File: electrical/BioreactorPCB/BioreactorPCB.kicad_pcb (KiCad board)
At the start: 2 copper layers, 81.5 x 56.5 mm, 68 parts, among them IC1 AL5809-20P1-7, IC2 VEML7700-TR, J1 61300311121, J10 USB_B, J11 Conn_01x06_Male, J12 Conn_02x03_Odd_Even, J13 PJ-202A, J14 Conn_01x05_Male, J2 61300311121, J3 Conn_01x05_Male, J4 Conn_01x06_Male, J5 OSTTC022162, J6 OSTTC022162, J7 OSTTC042162, J8 OSTTC042162, J9 OSTTC042162, Q1 2N3905, Q2 IRF540N, Q3 FQP47P06, Q4 TL2575HV-05IKV, U1 L293D, U2 FT232RL, U3 ATMEGA328P-AUR, U4 TCA39306DCUR, Y1 16 mHz

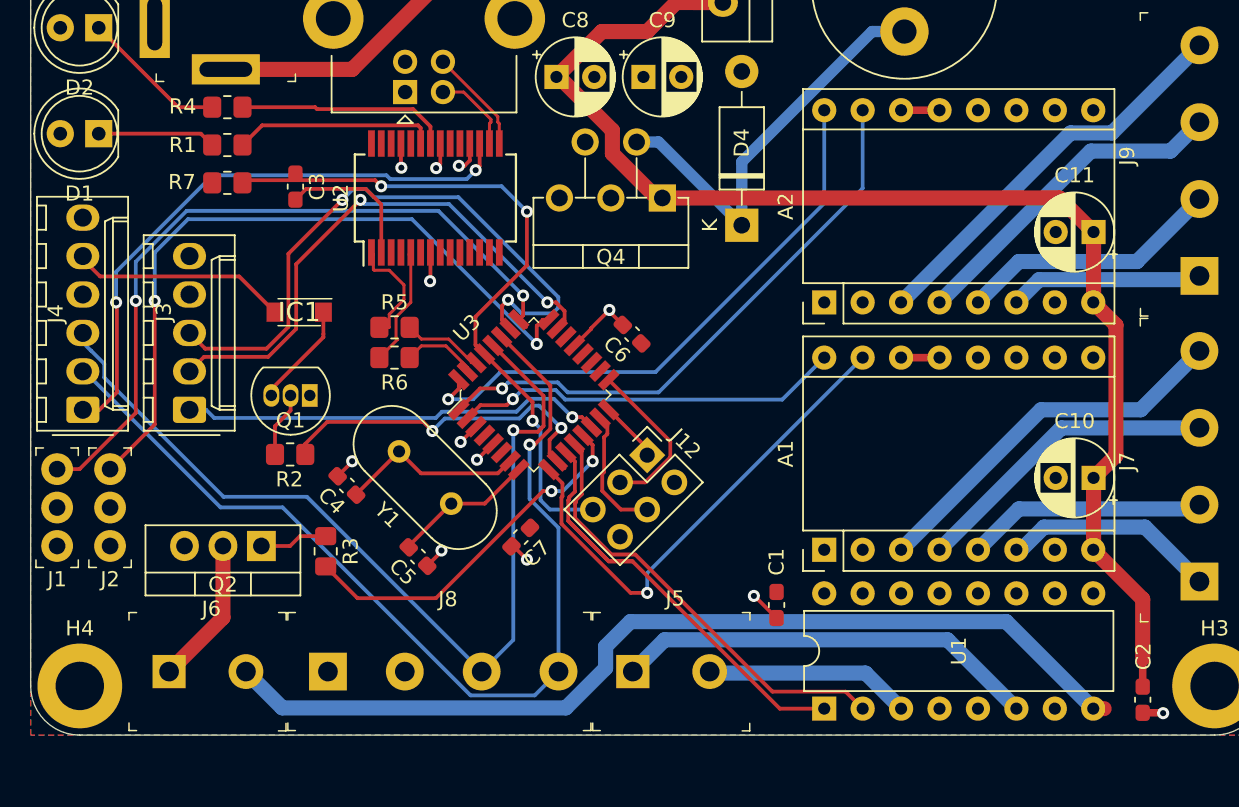
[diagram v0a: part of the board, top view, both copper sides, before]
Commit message: Moved around some traces for better planes
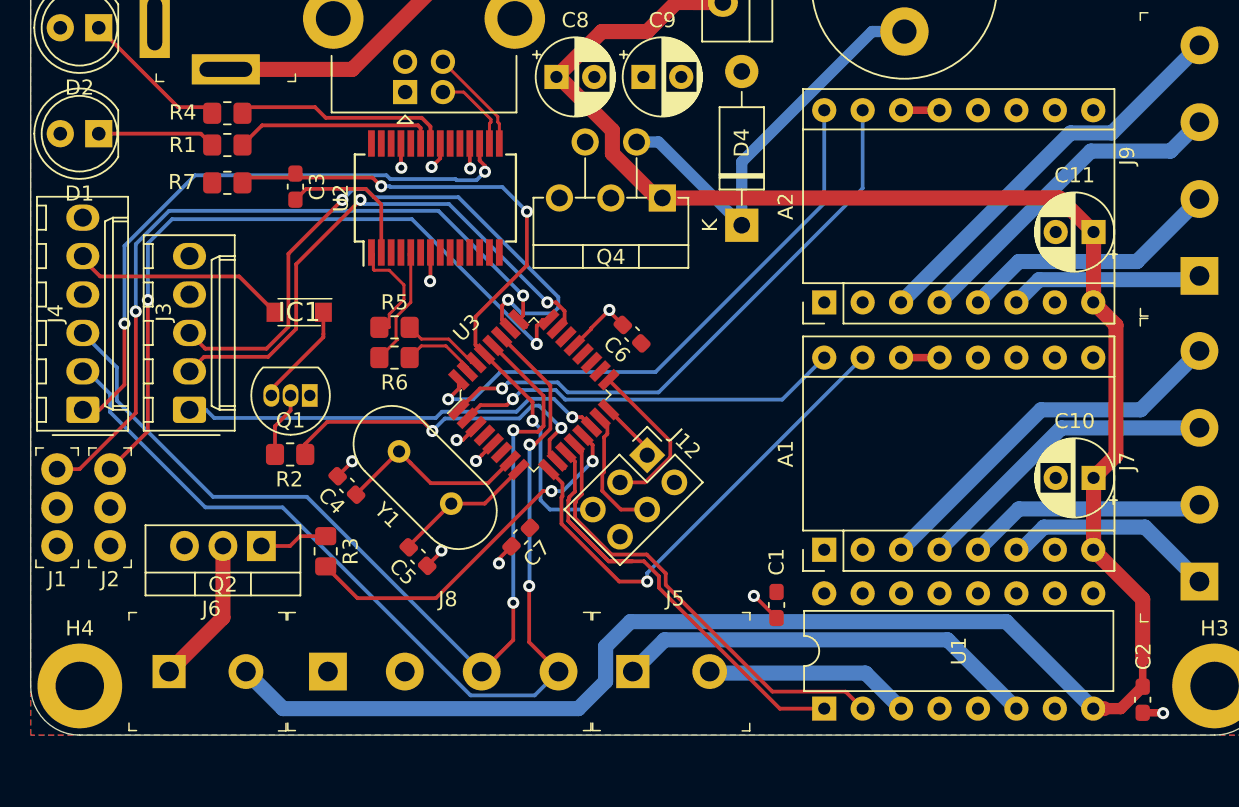
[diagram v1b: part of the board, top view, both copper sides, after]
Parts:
- moved R4 0.40 mm to (94.8, 52.9)
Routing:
- net +12V: track 151.6 -> 156.1 mm
- net +3V3: track 39.4 -> 40.8 mm
- net D5: track 33.0 -> 31.9 mm
- net SDA: track 66.8 -> 67.5 mm, vias 1 -> 2
- net TEMP_OUT: track 48.4 -> 49.1 mm
- net PH_OUT: track 47.3 -> 47.9 mm
- net XTAL+: track 12.3 -> 12.9 mm
- net SCL: track 62.2 -> 62.7 mm, vias 1 -> 2

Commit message: finished daughterboards
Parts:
- J11, J14, R8, U4: moved to B.Cu
- moved H6 118.4 mm to (114.2, 97.7), turned to 270 degrees
- moved H5 104.5 mm to (114.2, 117.7), turned to 270 degrees
- moved H10 98.9 mm to (85.0, 97.7), turned to 90 degrees
- moved R8 97.8 mm to (120.0, 102.5)
- moved U4 96.5 mm to (130.0, 102.3), turned to 180 degrees
- moved D3 87.2 mm to (114.2, 109.0), turned to 90 degrees
- moved H9 87.1 mm to (85.0, 117.7), turned to 90 degrees
- moved H12 84.4 mm to (107.5, 97.7), turned to 90 degrees
- moved J14 83.8 mm to (85.2, 112.8), turned to 90 degrees
- moved R10 81.7 mm to (90.5, 102.8), turned to 270 degrees
- moved R11 79.7 mm to (90.5, 112.7), turned to 90 degrees
- moved H11 77.1 mm to (107.5, 117.7), turned to 90 degrees
- moved H7 75.0 mm to (144.2, 97.7)
- moved R9 69.4 mm to (90.5, 107.7), turned to 90 degrees
- moved H8 66.2 mm to (144.2, 117.7)
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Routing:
- net Net-(J14-Pad3): track 0.00 -> 25.3 mm
- net Net-(J14-Pad2): track 0.00 -> 24.9 mm, vias 0 -> 1
- net 3V3_2: track 0.00 -> 21.7 mm
- net Net-(J14-Pad1): track 0.00 -> 18.3 mm
- net SCL1: track 0.00 -> 17.3 mm, vias 0 -> 1
- net Net-(D3-Pad2): track 0.00 -> 15.0 mm
- net SDA1: track 0.00 -> 12.9 mm, vias 0 -> 1
- net SDA2: track 0.00 -> 9.41 mm, vias 0 -> 1
- net Net-(R8-Pad2): track 0.00 -> 8.31 mm
- net 5V_3: track 0.00 -> 6.35 mm
- net SCL2: track 0.00 -> 6.09 mm
- net Net-(D4-Pad1): track 27.7 -> 28.3 mm
- net D2: track 37.9 -> 37.4 mm
- net GND2: vias 0 -> 1
- added copper zone on F.Cu, net 5V_2
- added copper zone on B.Cu, net GND2
- added copper zone on F.Cu, net GND2
- added copper zone on B.Cu, net GND3
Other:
- board size 81.5 x 56.5 mm -> 81.5 x 83.4 mm

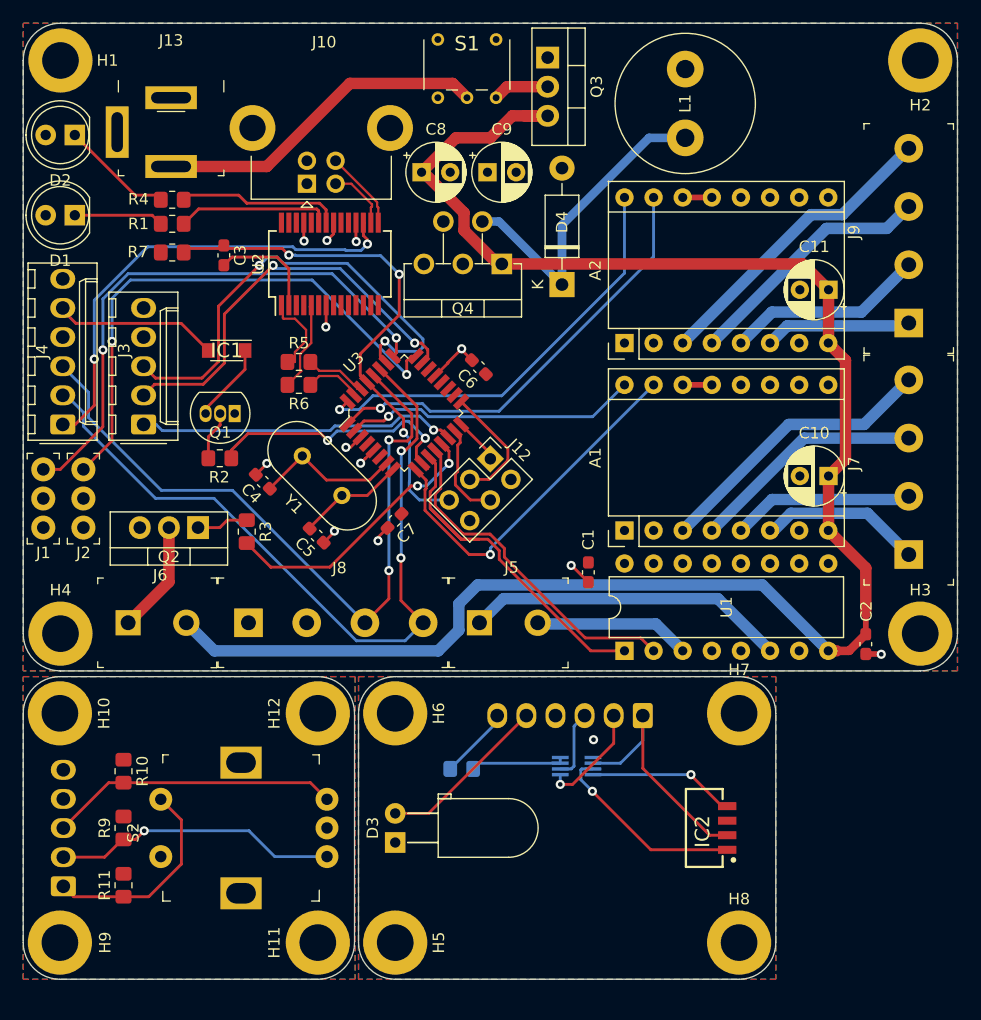
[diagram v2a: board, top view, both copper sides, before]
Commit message: panelized completed daughterboards and added clearance of planes to board edge
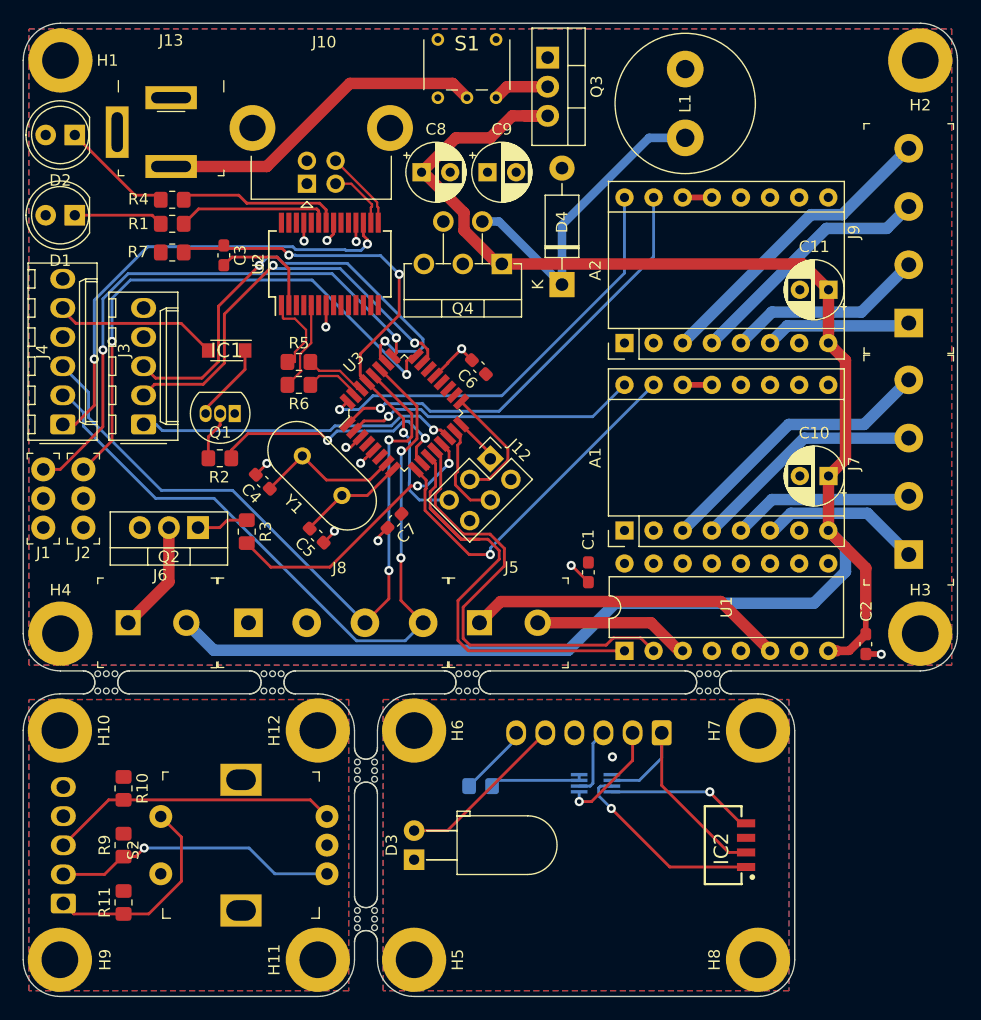
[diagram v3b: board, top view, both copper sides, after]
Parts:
- added mouse-bite-2mm-slot: VAL**, Panelization:mouse-bite-2mm-slot, F.Cu at (111.7, 115.7)
- added mouse-bite-2mm-slot: VAL**, Panelization:mouse-bite-2mm-slot, F.Cu at (111.7, 102.7)
- added mouse-bite-2mm-slot: VAL**, Panelization:mouse-bite-2mm-slot, F.Cu at (141.5, 95.0)
- added mouse-bite-2mm-slot: VAL**, Panelization:mouse-bite-2mm-slot, F.Cu at (120.5, 95.0)
- added mouse-bite-2mm-slot: VAL**, Panelization:mouse-bite-2mm-slot, F.Cu at (103.5, 95.0)
- added mouse-bite-2mm-slot: VAL**, Panelization:mouse-bite-2mm-slot, F.Cu at (89.0, 95.0)
- moved H7 2.23 mm to (145.8, 99.2), turned to 90 degrees
- moved H8 2.23 mm to (145.8, 119.2), turned to 90 degrees
- moved IC2 2.23 mm to (144.4, 112.6)
- moved R8 2.23 mm to (121.7, 104.0)
- moved U4 2.23 mm to (131.7, 103.8)
- moved D3 2.23 mm to (115.8, 110.5)
- moved H5 2.23 mm to (115.8, 119.2)
- moved H6 2.23 mm to (115.8, 99.2)
- moved J11 2.23 mm to (137.4, 99.4)
- moved H10 1.50 mm to (85.0, 99.2)
- moved H11 1.50 mm to (107.5, 119.2)
- moved H12 1.50 mm to (107.5, 99.2)
- moved H9 1.50 mm to (85.0, 119.2)
- moved J14 1.50 mm to (85.2, 114.3)
- moved R10 1.50 mm to (90.5, 104.2)
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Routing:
- net D8: track 30.0 -> 39.7 mm
- net D7: track 33.5 -> 42.8 mm
- net +12V: track 156.1 -> 158.5 mm
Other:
- board size 81.5 x 83.4 mm -> 81.5 x 84.9 mm

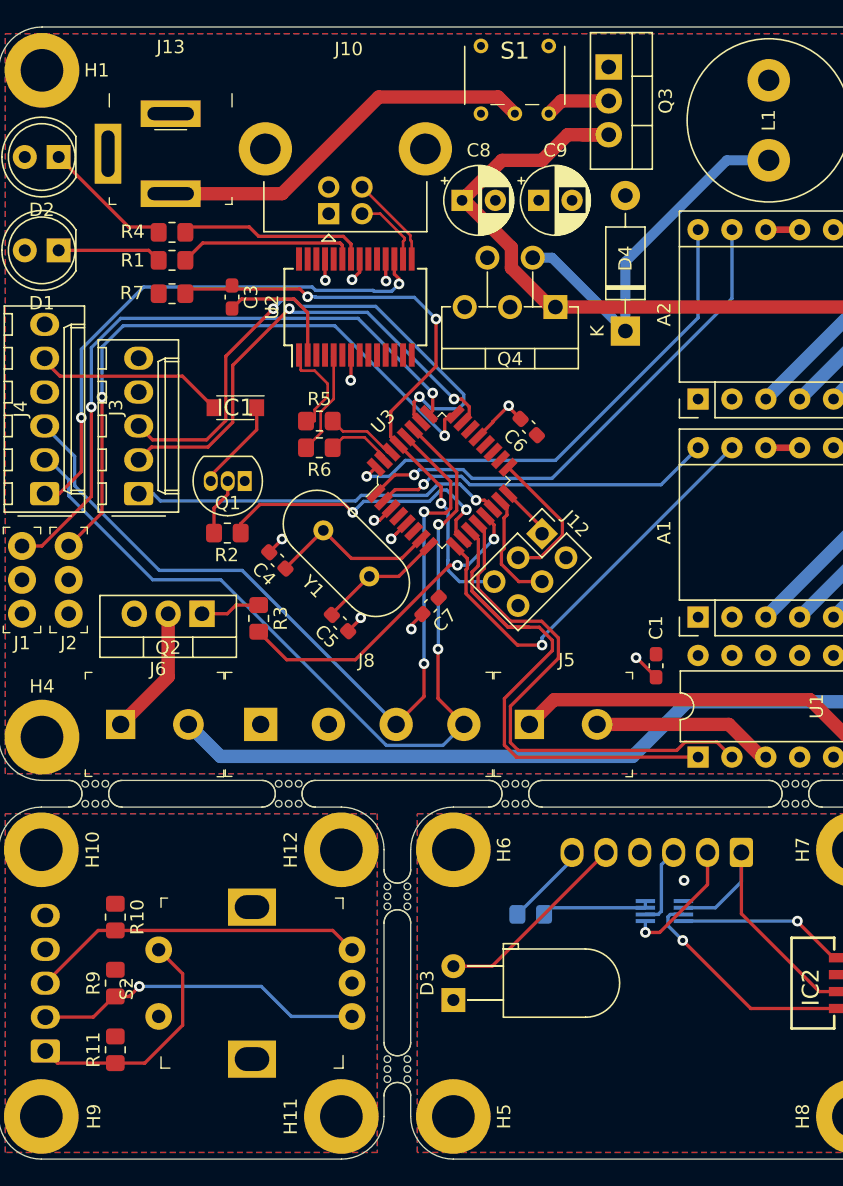
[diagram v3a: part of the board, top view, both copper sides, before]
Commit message: added silk labels
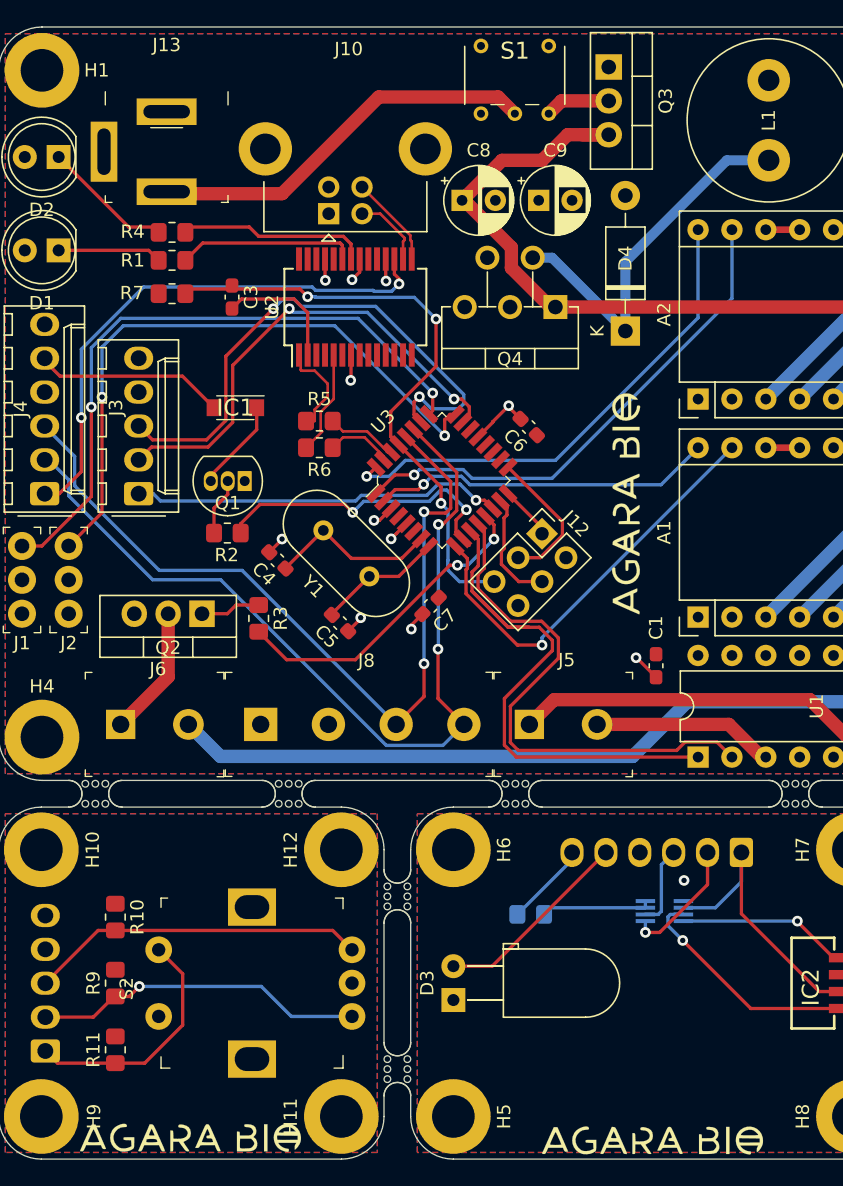
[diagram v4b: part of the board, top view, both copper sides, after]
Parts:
- added G***: LOGO, AgaraLogo:AgaraLogoSmall, F.Cu at (128.8, 73.2)
- added G***: LOGO, AgaraLogo:AgaraLogoSmall, F.Cu at (96.2, 120.8)
- added G***: LOGO, AgaraLogo:AgaraLogoSmall, F.Cu at (130.8, 121.0)
- moved J13 0.34 mm to (94.3, 46.9)
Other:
- board text added: "Design by Sreenivas Eadara"
